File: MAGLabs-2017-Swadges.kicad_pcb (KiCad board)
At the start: 2 copper layers, 70 x 120 mm, 37 parts, among them J1 LCD Screen, J2 IR Sensor, J3 Program, U1 ESP12E

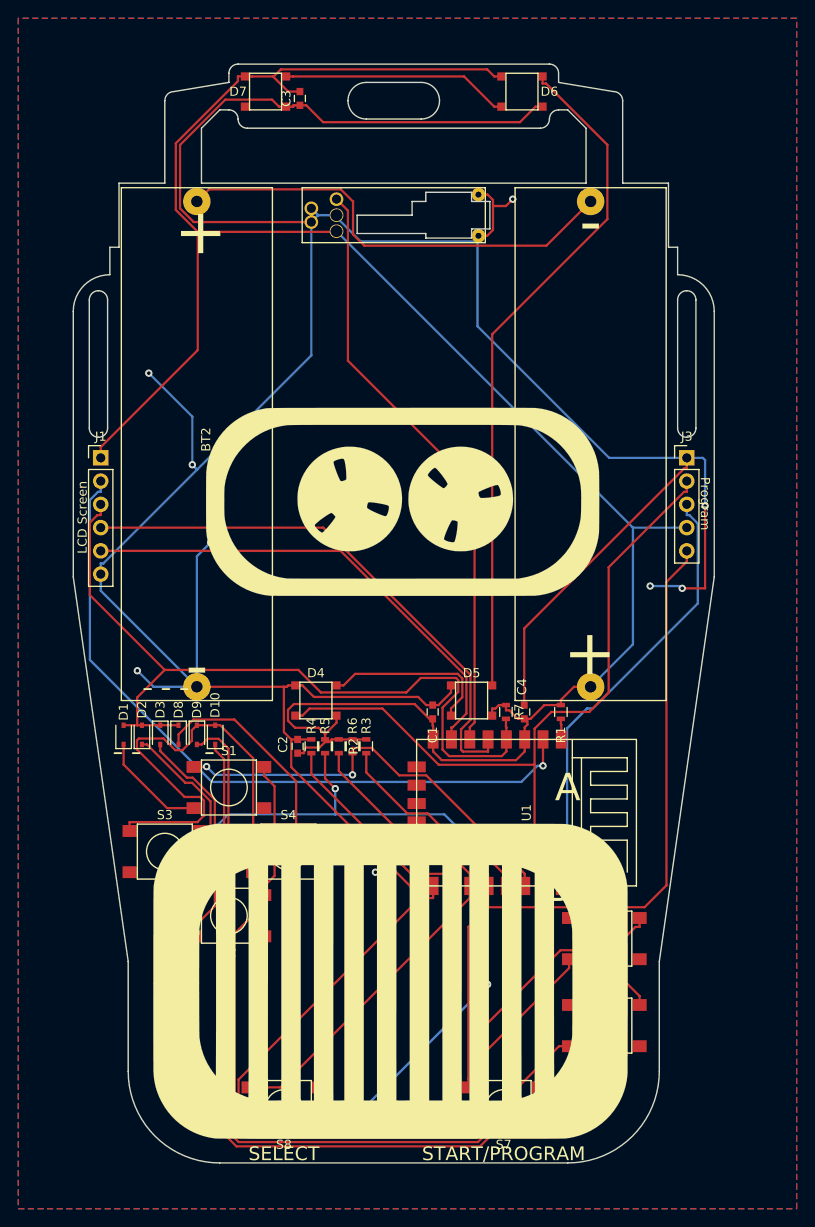
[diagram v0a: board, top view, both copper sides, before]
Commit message: Adjusted vive sensor, moved art to silkscreen
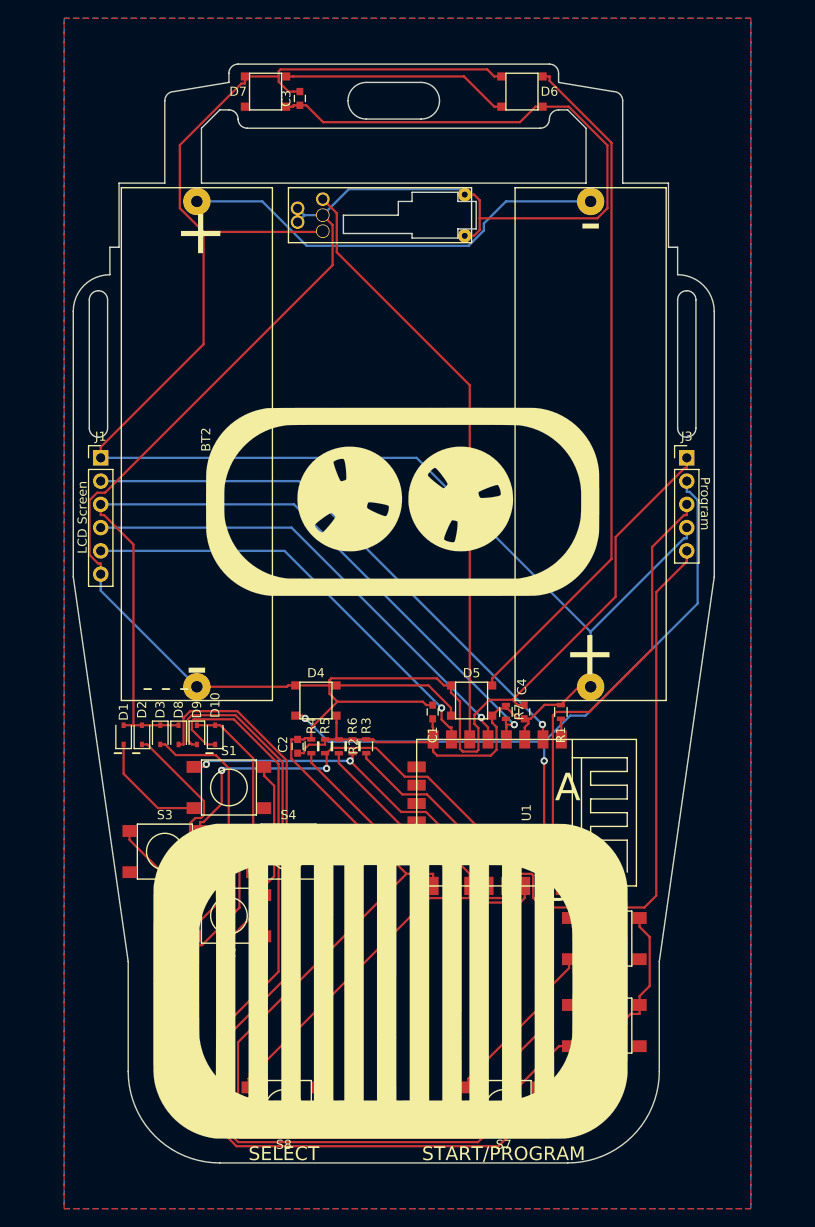
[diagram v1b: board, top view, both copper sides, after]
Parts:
- moved J2 1.50 mm to (134.5, 51.5)
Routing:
- net GND: track 460.9 -> 344.7 mm, vias 13 -> 0
- net Net-(J1-Pad2): track 78.8 -> 60.9 mm
- net Net-(D10-Pad1): track 87.1 -> 101.1 mm
- net Net-(D9-Pad2): track 97.8 -> 109.1 mm
- net +3V3: track 235.9 -> 228.6 mm
- net Net-(J1-Pad4): track 60.0 -> 52.9 mm, vias 0 -> 1
- net GPIO0: track 102.1 -> 109.2 mm
- net Net-(S1-Pad2): track 111.0 -> 106.0 mm
- net Net-(J1-Pad5): track 53.2 -> 48.3 mm, vias 0 -> 1
- net Net-(D4-Pad2): track 19.0 -> 14.4 mm
- net Net-(D3-Pad2): track 24.8 -> 28.5 mm
- net Net-(BT1-Pad2): track 50.2 -> 47.5 mm
- net Net-(D8-Pad2): track 28.6 -> 31.1 mm
- net Net-(R5-Pad2): track 47.2 -> 49.3 mm, vias 3 -> 2
- net RXD: track 83.1 -> 81.2 mm, vias 0 -> 2
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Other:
- outline, holes or cut-outs redrawn

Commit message: Citizen
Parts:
- added G***: LOGO, local:SUNNY, F.Cu at (157.5, 76.2)
- added G***: LOGO, local:Citizen-label, B.Cu at (136.0, 119.0)
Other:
- rule pad_to_mask_clearance: 0.2 -> 0.1
- board text added: "SUNNY IS A VERY NICE KITTY"

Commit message: All prod files
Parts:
- removed the G*** at (136.0, 119.0)
- added G***: LOGO, local:Guest-label2, B.Cu at (137.5, 118.8)
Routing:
- net GND: track 344.7 -> 357.8 mm, vias 0 -> 4
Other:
- board text added: "Charles Lohr"
- board text added: "MAGLabs 2017"
- board text added: "Mark Murnane"

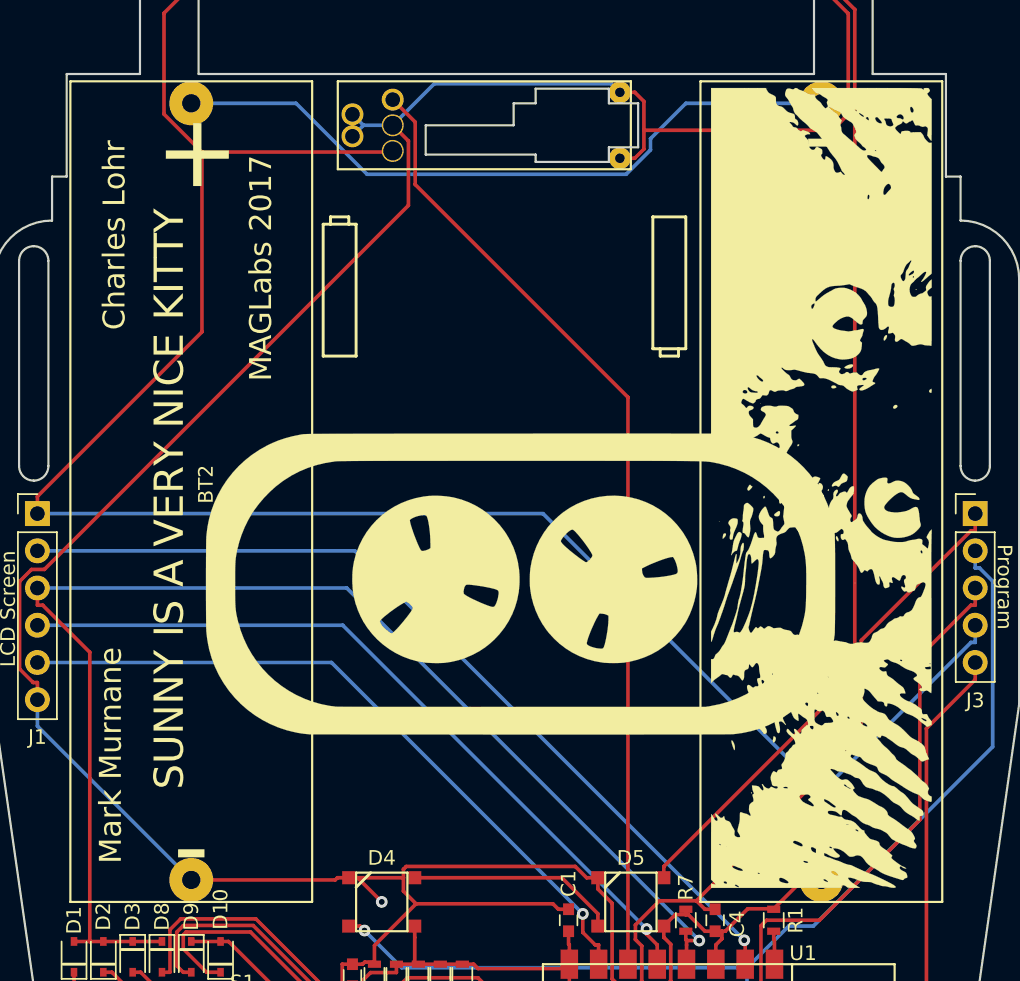
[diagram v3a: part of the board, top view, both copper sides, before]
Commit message: Add citizen2 + update outputs
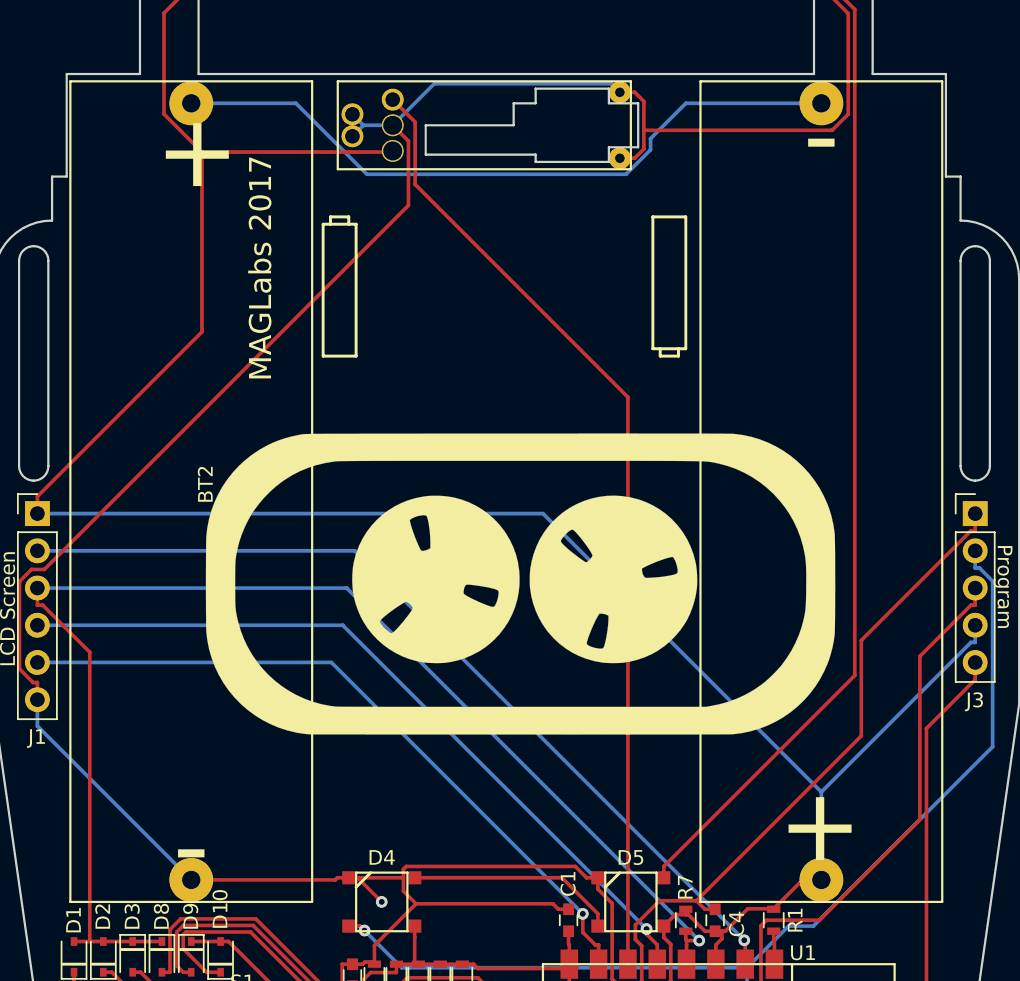
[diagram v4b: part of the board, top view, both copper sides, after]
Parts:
- removed the G*** at (137.5, 118.8)
- removed the G*** at (157.5, 76.2)
- added G***: LOGO, mark:Citizen-label2, B.Cu at (136.1, 119.7)
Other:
- board text removed: "Charles Lohr"
- board text removed: "Mark Murnane"
- board text removed: "SUNNY IS A VERY NICE KITTY"
